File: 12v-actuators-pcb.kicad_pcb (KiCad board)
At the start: 2 copper layers, 248.3 x 109.6 mm, 213 parts, among them J1 690367280876, J10 ESC_35_1_P, J11 690367280876, J12 ESC_35_2_S, J13 Alim Pompe, J14 690367280876, J16 690367280876, J17 690367280876, J18 690367280876, J19 Alim EV, J2 3.5mm WR-TBL, J20 Alim EV, J21 Alim EV, J22 Alim EV, J23 Alim EV, J24 Alim EV, J25 Alim EV, J26 Alim EV, J27 Alim EV, J28 Alim EV, J29 Alim EV, J3 690367280676, J30 Alim EV, J4 STLINK, J5 USB_B_Mini, J6 ESC_35_1_P, J7 RGBA_LEDs, J8 CAN, J9 ESC_35_1_S, Q1 G2302, Q10 G2302, Q11 G2302, Q12 G2302, Q13 G2302, Q14 G2302, Q15 G2302, Q16 G2302, Q17 G2302, Q18 G2302, Q2 G2302, Q3 G2302, Q4 G2302, Q5 G2302, Q6 SUM110P06-08L, Q7 2N7002, Q8 2N7002, SW1 435431019840, U1 MCP2551-I-SN, U2 TCA9517DR, U3 WSEN-PDUS, U4 STM32G474CEUx, U5 AMS1117-3.3, U6 TPS82130, Y1 16 MHz

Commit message: nettoyage dossier et assignation de ref JLCPCB
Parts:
- removed H10, H5, H6, H7, H8, H9: MountingHole_Pad, MountingHole:MountingHole_3.2mm_M3_Pad
- added C31: 1uF, Capacitor_SMD:C_0805_2012Metric, F.Cu at (117.0, 116.5)
- added FID1: Fiducial, Fiducial:Fiducial_0.5mm_Mask1mm, F.Cu at (157.2, 60.5)
- added FID2: Fiducial, Fiducial:Fiducial_0.5mm_Mask1mm, F.Cu at (178.7, 127.0)
- added FID3: Fiducial, Fiducial:Fiducial_0.5mm_Mask1mm, F.Cu at (118.7, 133.5)
- C22, C26: value 15nF -> 10nF
- C24: value 220nF -> 100nF
- C7: value 430pF -> 470pF
- C9: footprint Capacitor_SMD:C_0603_1608Metric -> Capacitor_SMD:C_0805_2012Metric
- D6: value ~ -> RS3J R6
- D7: value 14.6V -> MM3Z15VST1G
- J5: value USB_B_Mini -> 65100516121
- U5: footprint Package_TO_SOT_SMD:SOT-89-3 -> Package_TO_SOT_SMD:SOT-223-3_TabPin2
- moved D12 139.6 mm to (123.0, 62.5)
- moved D13 139.6 mm to (129.5, 62.5)
- moved D14 139.6 mm to (148.0, 62.5)
- moved D19 139.6 mm to (154.5, 62.5)
- moved J17 139.6 mm to (139.0, 60.0)
- moved J24 139.6 mm to (155.8, 66.0)
- moved J25 139.6 mm to (124.2, 66.0)
- moved J26 139.6 mm to (134.8, 66.0)
- moved J27 139.6 mm to (145.2, 66.0)
- moved Q10 139.6 mm to (129.5, 59.0)
- moved Q11 139.6 mm to (148.0, 59.0)
- moved Q15 139.6 mm to (123.0, 59.0)
- moved Q18 139.6 mm to (154.5, 59.0)
- moved R36 139.6 mm to (125.5, 58.0)
- moved R37 139.6 mm to (132.0, 58.0)
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- renumbered R64 to R53, R78 to R54, R79 to R55, R80 to R56, R81 to R57, R82 to R58, R86 to R59, R87 to R60, R88 to R61, R89 to R62
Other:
- board size 248.3 x 109.6 mm -> 83 x 80 mm

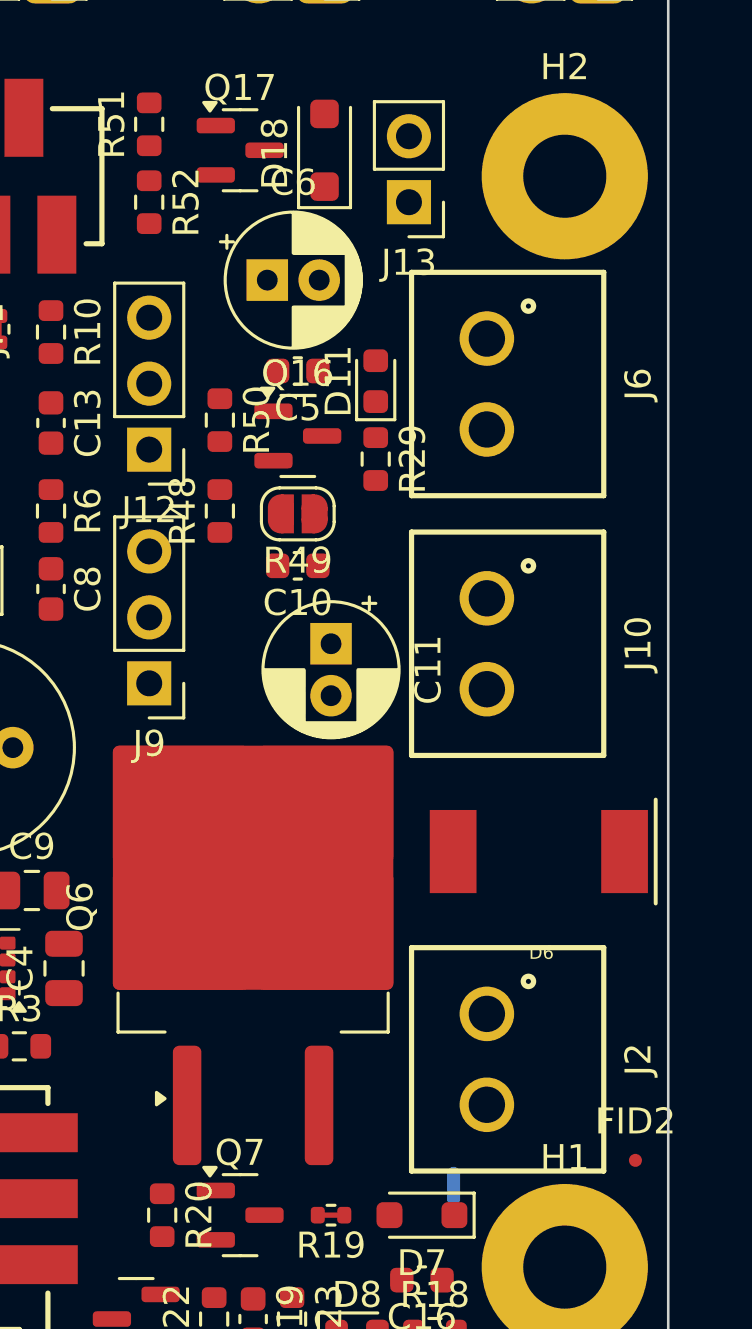
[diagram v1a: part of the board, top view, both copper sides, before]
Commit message: Correction orientation conn alim
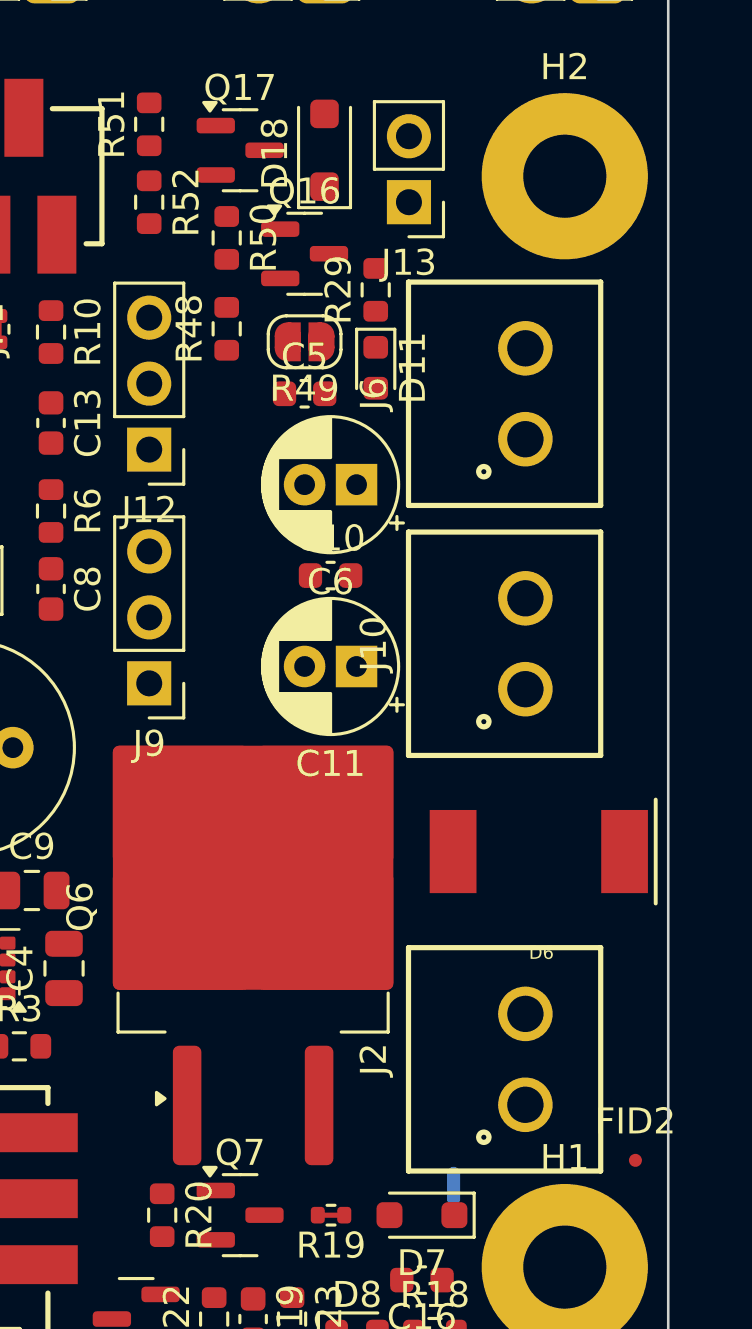
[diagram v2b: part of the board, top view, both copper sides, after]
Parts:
- moved C6 8.59 mm to (168.0, 101.0), turned to 180 degrees
- moved Q16 7.02 mm to (166.0, 92.1)
- moved R48 7.02 mm to (163.0, 95.0)
- moved R50 7.02 mm to (163.0, 91.5)
- moved R49 6.63 mm to (166.0, 95.5)
- moved R29 6.51 mm to (168.7, 93.5), turned to 90 degrees
- moved J6 1.53 mm to (174.5, 97.5), turned to 90 degrees
- moved J10 1.48 mm to (174.5, 107.1), turned to 90 degrees
- moved J2 1.48 mm to (174.5, 123.1), turned to 90 degrees
- moved C10 1.32 mm to (167.0, 104.5), turned to 0 degrees
- moved C11 1.32 mm to (168.0, 108.0), turned to 180 degrees
- moved C5 0.91 mm to (166.0, 97.5), turned to 0 degrees
- moved D11 0.51 mm to (168.7, 96.5), turned to -90 degrees

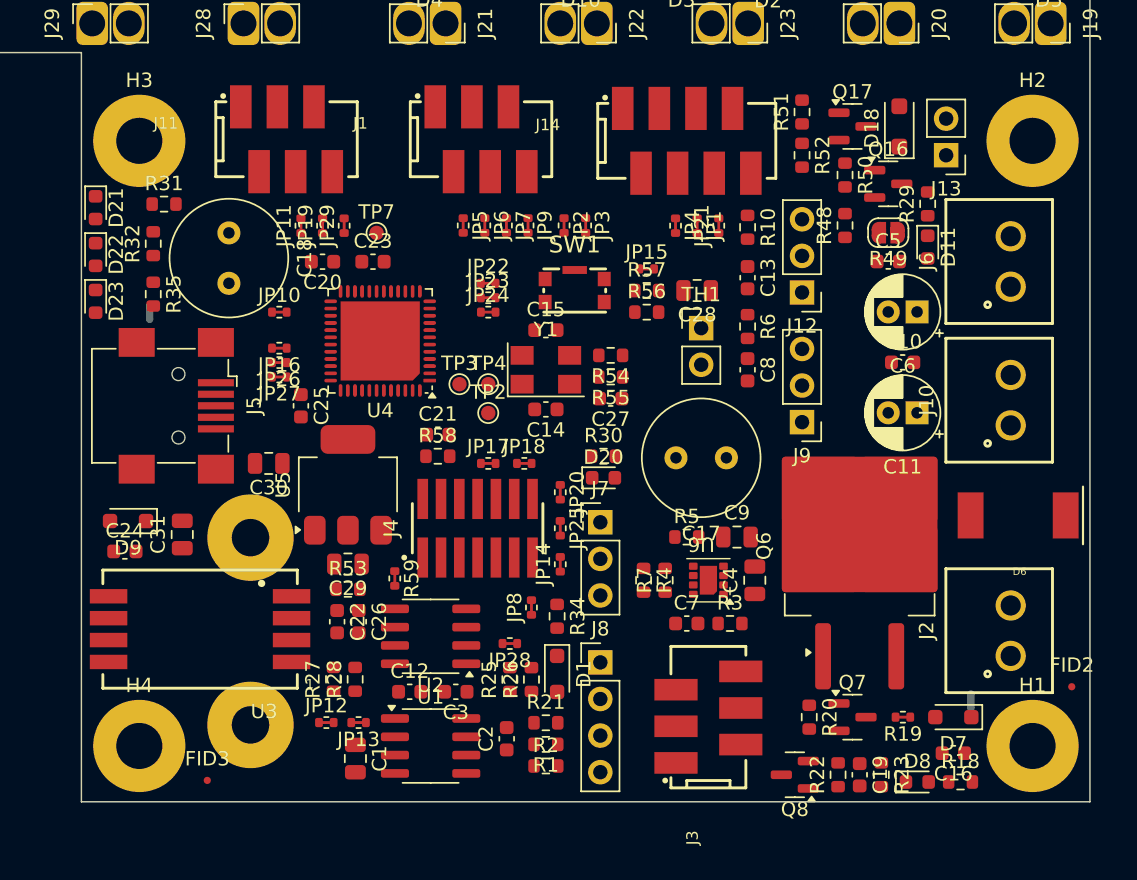
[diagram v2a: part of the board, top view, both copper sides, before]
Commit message: debut du tracee des pistes (et modification de l'empreinte R_0402_1005Metric_jumperClosed.kicad_mod pour que le DRC accepte de la router
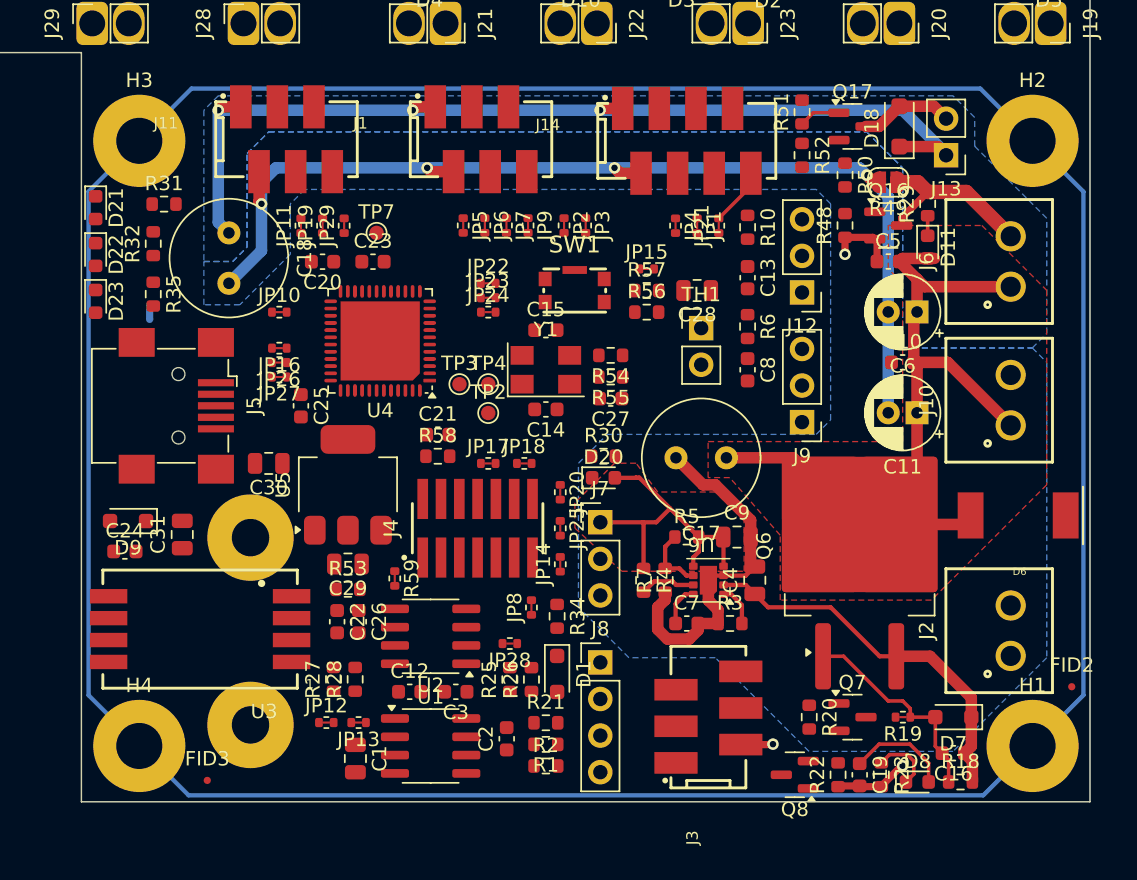
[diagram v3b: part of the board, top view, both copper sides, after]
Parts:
- moved R49 3.50 mm to (166.0, 92.0)
- moved Q16 2.89 mm to (166.0, 95.0)
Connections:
- net /MCU et capteurs/USB_DN_J renamed /MCU et capteurs/USB_J_N
- net /MCU et capteurs/USB_DP_J renamed /MCU et capteurs/USB_J_P
- net /USB_DN renamed /USB_N
- net /USB_DP renamed /USB_P
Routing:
- net GND: track 0.00 -> 227.1 mm, vias 0 -> 2
- net /PWR_12V: track 0.00 -> 126.6 mm, vias 0 -> 3
- net GNDPWR: track 0.00 -> 105.1 mm, vias 0 -> 5
- net /VBATT_12V: track 0.00 -> 26.7 mm
- net +5VP: track 0.00 -> 21.9 mm
- net Net-(D7-A): track 0.00 -> 14.8 mm
- net Net-(J6-Pin_2): track 0.00 -> 12.5 mm
- net /Alim et Arrêt d'urgence/SW_AU/2: track 0.00 -> 7.21 mm
- net /Actionneurs/12V_VAC: track 0.00 -> 6.50 mm
- net Net-(U6-FB): track 0.00 -> 4.61 mm
- net Net-(D8-K): track 0.00 -> 4.36 mm
- net /EV_P: track 0.00 -> 4.05 mm
- net Net-(U6-PG): track 0.00 -> 3.86 mm
- net Net-(Q17-G): track 0.00 -> 2.88 mm
- net /LED_EN: track 0.00 -> 2.87 mm
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- added copper zone on F.Cu, net +5VP
- added copper zone on B.Cu, net /PWR_12V
- added copper zone on F.Cu, net /PWR_12V
- added copper zone on B.Cu, net GNDPWR

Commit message: Minor adjust before routing
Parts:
- moved R24 14.5 mm to (126.5, 92.5)
- moved R62 4.14 mm to (169.5, 131.5)
- moved J16 0.80 mm to (167.5, 74.2)
- moved J17 0.80 mm to (139.0, 59.2)
- moved J18 0.80 mm to (109.5, 74.2)
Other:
- outline, holes or cut-outs redrawn
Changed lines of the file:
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@@
 	(footprint "ConnectorsEvo:690367280676"
 		(layer "F.Cu")
-		(at 139 60)
+		(at 139 59.2)
 		(descr "<b>WR-MM</b><br> Female SMT Connector with Polarization, 6Pins")
 		(property "Reference" "J17"
@@
 	(footprint "ConnectorsEvo:690367280876"
 		(layer "F.Cu")
-		(at 167.525 74.95)
+		(at 167.525 74.15)
 		(descr "<b>WR-MM</b><br> Female SMT Connector with Polarization, 8 pins")
 		(property "Reference" "J16"
@@
 	(footprint "ConnectorsEvo:690367280676"
 		(layer "F.Cu")
-		(at 109.5 75)
+		(at 109.5 74.2)
 		(descr "<b>WR-MM</b><br> Female SMT Connector with Polarization, 6Pins")
 		(property "Reference" "J18"
@@
 	(footprint "NetTie:NetTie-2_SMD_Pad0.5mm"
 		(layer "B.Cu")
-		(at 114.7372 101.0148 -90)
+		(at 126.5 92.5 -90)
 		(descr "Net tie, 2 pin, 0.5mm square SMD pads")
 		(tags "net tie")
@@
 	(footprint "NetTie:NetTie-2_SMD_Pad0.5mm"
 		(layer "B.Cu")
-		(at 171.7372 128.0148 -90)
+		(at 169.5 131.5 -90)
 		(descr "Net tie, 2 pin, 0.5mm square SMD pads")
 		(tags "net tie")
@@
 		(stroke
 			(width 0.1)
+			(type default)
+		)
+		(layer "Edge.Cuts")
+	)
+	(gr_arc
+		(start 132 83)
+		(mid 133 84)
+		(end 132 85)
+		(stroke
+			(width 0.1)
+			(type default)
+		)
+		(layer "Edge.Cuts")
+	)
+	(gr_arc
+		(start 155.5 85)
+		(mid 154.5 84)
+		(end 155.5 83)
+		(stroke
+			(width 0.1)
+			(type default)
+		)
+		(layer "Edge.Cuts")
+	)
+	(gr_arc
+		(start 149 83)
+		(mid 150 84)
+		(end 149 85)
+		(stroke
+			(width 0.1)
+			(type default)
+		)
+		(layer "Edge.Cuts")
+	)
+	(gr_arc
+		(start 137.5 85)
+		(mid 136.5 84)
+		(end 137.5 83)
+		(stroke
+			(width 0.1)

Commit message: Routing 40%
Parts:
- moved R21 1.54 mm to (142.5, 128.0)
- moved C2 1.15 mm to (139.8, 129.5), turned to 180 degrees
- moved JP28 1.13 mm to (139.2, 123.0), turned to -90 degrees
- moved JP8 1.11 mm to (140.2, 121.0)
- moved R1 1.05 mm to (143.2, 130.8), turned to 90 degrees
- moved R25 1.04 mm to (138.8, 126.2)
- moved R26 1.04 mm to (140.2, 126.2)
- moved C21 0.92 mm to (135.2, 108.8), turned to -90 degrees
- moved R2 0.91 mm to (141.8, 131.8), turned to -90 degrees
- moved D1 0.91 mm to (143.2, 125.2)
- moved JP9 0.84 mm to (140.2, 94.6)
- moved TP2 0.71 mm to (137.8, 107.5)
- moved JP12 0.62 mm to (126.5, 129.1), turned to 90 degrees
- moved JP7 0.62 mm to (139.0, 94.6)
- moved JP13 0.61 mm to (128.8, 129.1), turned to 90 degrees
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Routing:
- net +3.3V: track 0.00 -> 75.8 mm
- net GND: track 227.1 -> 293.9 mm, vias 2 -> 6
- net /MCU et capteurs/SCL_J: track 0.00 -> 40.2 mm, vias 0 -> 2
- net +5VL: track 0.00 -> 28.2 mm
- net /MCU et capteurs/CAN_TX_J: track 0.00 -> 25.4 mm, vias 0 -> 2
- net /MCU et capteurs/CAN_RX_J: track 0.00 -> 24.3 mm, vias 0 -> 2
- net /MCU et capteurs/EV_P_J: track 0.00 -> 22.8 mm, vias 0 -> 2
- net /MCU et capteurs/A_PRES: track 0.00 -> 22.1 mm, vias 0 -> 2
- net /MCU et capteurs/EV_4_J: track 0.00 -> 22.1 mm, vias 0 -> 2
- net /MCU et capteurs/SWDIO: track 0.00 -> 21.3 mm, vias 0 -> 2
- net /MCU et capteurs/LED_DBG_1: track 0.00 -> 21.1 mm
- net /MCU et capteurs/EV_3_J: track 0.00 -> 20.9 mm
- net /MCU et capteurs/SDA_J: track 0.00 -> 20.1 mm, vias 0 -> 2
- net /MCU et capteurs/LED_DBG_2: track 0.00 -> 19.2 mm
- net /MCU et capteurs/LED_EN_J: track 0.00 -> 19.2 mm, vias 0 -> 2
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
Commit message: Routing 41%
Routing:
- net /EV_9: track 14.3 -> 51.9 mm, vias 0 -> 3
- net /EV_10: track 3.39 -> 35.7 mm
- net /EV_11: track 7.99 -> 35.5 mm
- net GNDPWR: track 105.1 -> 129.6 mm
- net /PWR_12V: track 126.6 -> 133.1 mm
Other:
- outline, holes or cut-outs redrawn

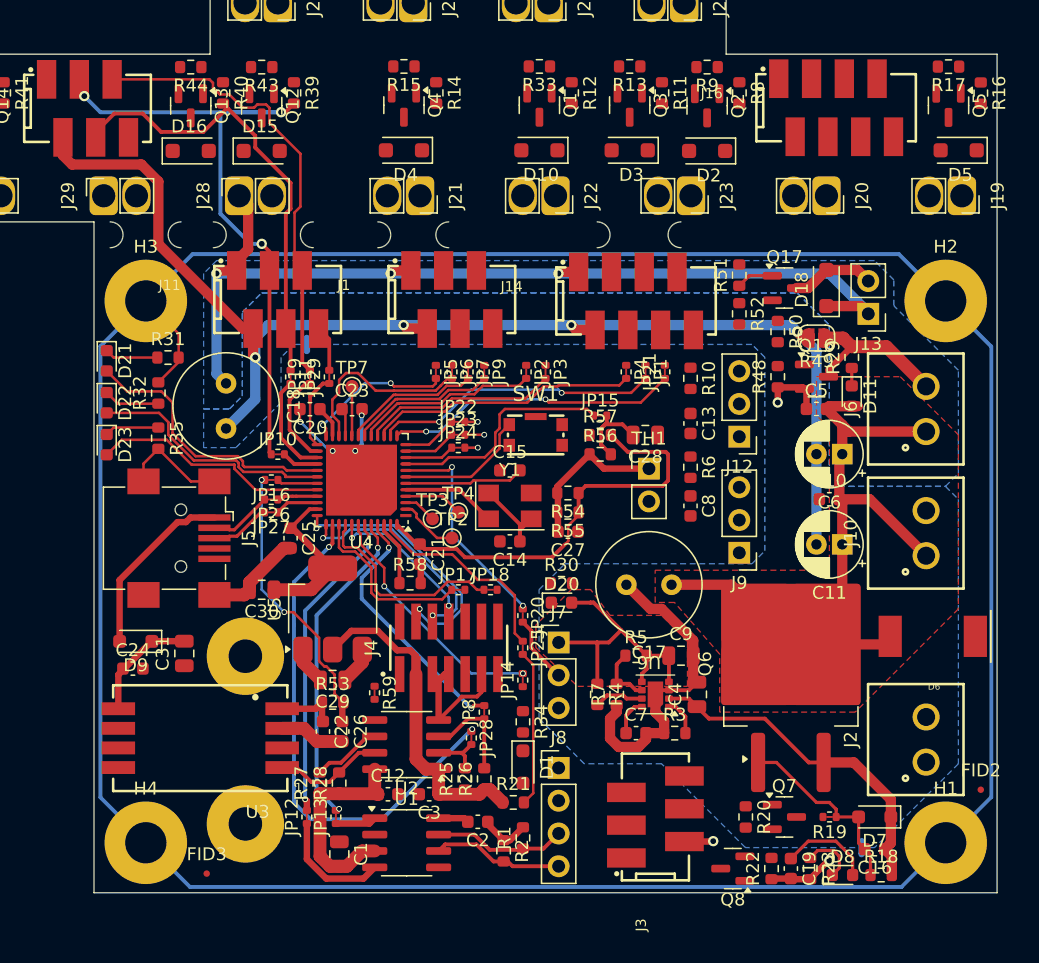
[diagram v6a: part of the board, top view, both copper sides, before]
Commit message: fin tracer piste et plan carte principale - mise a jour regle ERC sur la base de la carte Pneuma 2023 et alim 2020 - no ERC
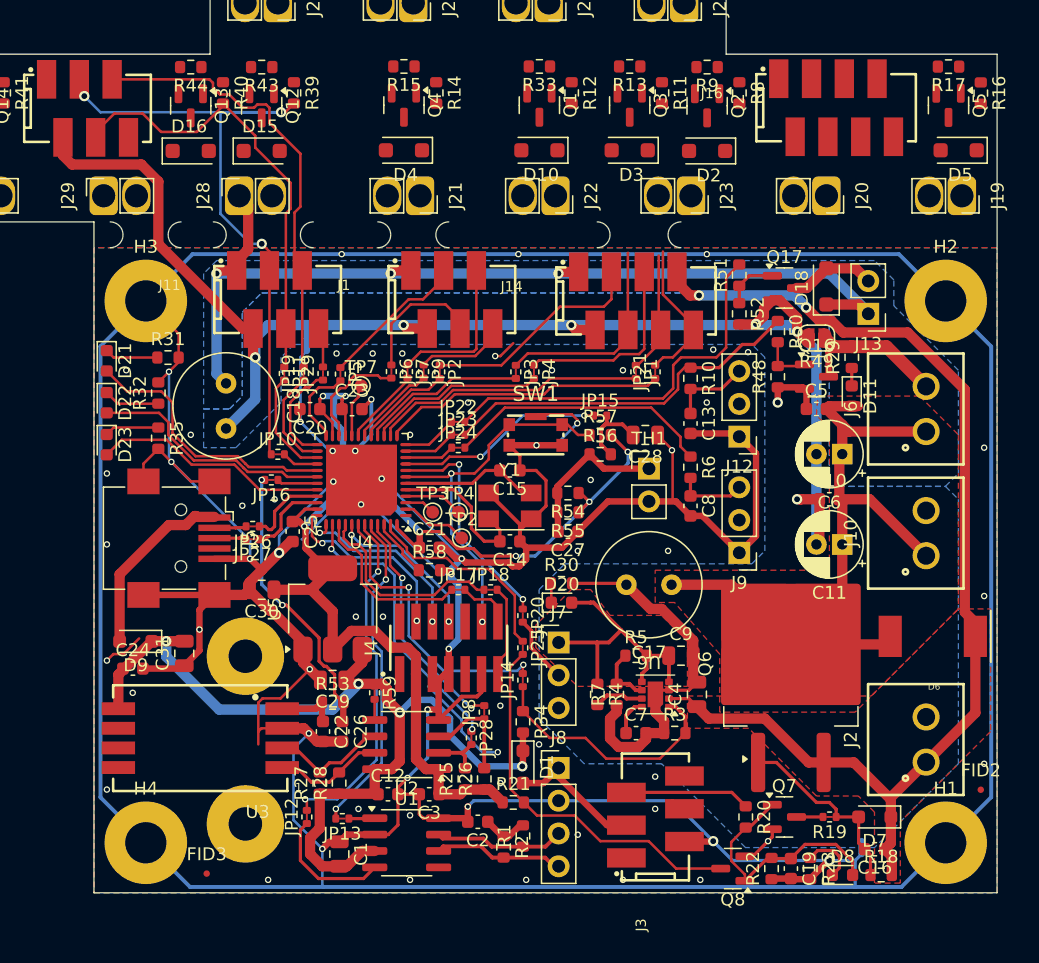
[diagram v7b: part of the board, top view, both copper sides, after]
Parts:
- moved JP5 7.40 mm to (129.1, 94.8)
- moved JP4 7.15 mm to (144.1, 94.6)
- moved JP2 6.70 mm to (136.8, 94.6)
- moved JP6 4.70 mm to (133.1, 94.6)
- moved JP7 4.70 mm to (134.3, 94.6)
- moved JP9 4.70 mm to (135.6, 94.6)
- moved JP26 2.53 mm to (122.3, 106.6)
- moved JP27 2.53 mm to (122.3, 107.6)
- moved JP3 2.30 mm to (142.7, 94.6)
- moved R58 1.80 mm to (136.0, 110.0)
- moved C21 0.90 mm to (136.0, 108.2), turned to 0 degrees
- moved JP1 0.75 mm to (152.0, 94.6)
- moved JP21 0.75 mm to (153.5, 94.6)
- moved TP2 0.75 mm to (138.5, 107.5)
- moved TP7 0.70 mm to (130.7, 95.7)
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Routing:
- net GND: track 293.9 -> 550.9 mm, vias 6 -> 71
- net /VBATT_12V: track 26.7 -> 88.2 mm, vias 0 -> 2
- net +5VL: track 28.2 -> 75.0 mm, vias 0 -> 4
- net /VAC: track 1.00 -> 30.6 mm, vias 1 -> 0
- net /DS_TURB: track 1.50 -> 28.6 mm, vias 1 -> 0
- net +3.3V: track 75.8 -> 100.3 mm, vias 0 -> 7
- net GNDPWR: track 129.6 -> 151.0 mm, vias 5 -> 8
- net /DS_COMP: track 1.00 -> 20.8 mm, vias 1 -> 0
- net /MCU et capteurs/NRST: track 10.3 -> 29.5 mm, vias 0 -> 2
- net /MCU et capteurs/SCL_J: track 40.2 -> 22.3 mm
- net /AU_STATUS: track 12.1 -> 29.7 mm
- net /EV_1: track 0.00 -> 17.5 mm
- net /LED_EN: track 2.87 -> 19.7 mm
- net /EV_2: track 0.00 -> 16.2 mm
- net /EV_3: track 0.00 -> 15.1 mm
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- added copper zone on F.Cu, net /VBATT_12V
- added copper zone on B.Cu, net GND
- added copper zone on F.Cu, net GND
